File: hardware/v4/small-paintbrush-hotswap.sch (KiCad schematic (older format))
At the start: 17 parts, among them J1 Conn_01x02, J2 Conn_01x04, J3 Conn_01x04, SW1 SW_SPDT, SW2 SW_SPDT, U1 ProMicro, U2 ProMicro

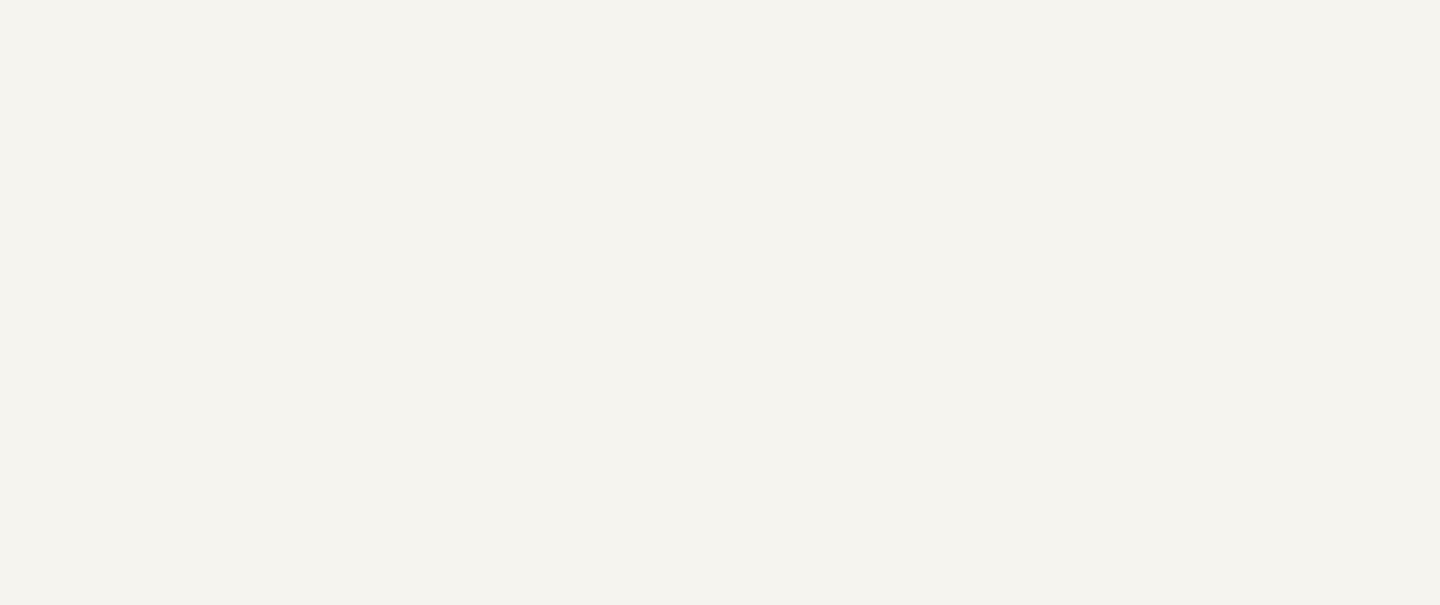
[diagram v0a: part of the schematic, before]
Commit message: Rev v4 to add tap holes
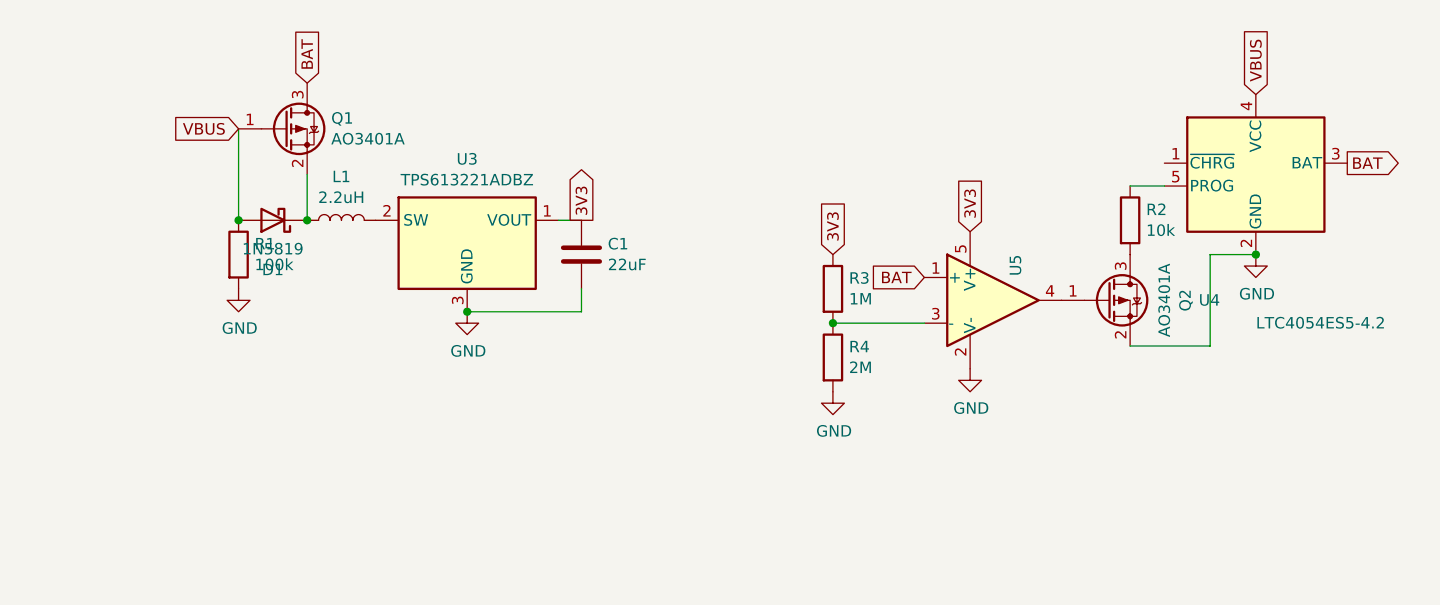
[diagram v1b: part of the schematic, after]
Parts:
- added C1: 22uF, symbol Device:C
- added D1: 1N5819, Diode_THT:D_DO-41_SOD81_P10.16mm_Horizontal, symbol Diode:1N5819
- added L1: 2.2uH, symbol Device:L
- added Q1, Q2: AO3401A, Package_TO_SOT_SMD:SOT-23, symbol Transistor_FET:AO3401A
- added R1: 100k, symbol Device:R
- added R2: 10k, symbol Device:R
- added R3: 1M, symbol Device:R
- added R4: 2M, symbol Device:R
- added U3: TPS613221ADBZ, Package_TO_SOT_SMD:SOT-23, symbol Regulator_Switching:TPS613221ADBZ
- added U4: LTC4054ES5-4.2, Package_TO_SOT_SMD:TSOT-23-5, symbol Battery_Management:LTC4054ES5-4.2
- added U5: LMV7271, symbol Comparator:LMV7271
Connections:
- net GND: now also C1.2, Q2.2 (S), R1.2, R4.2, U3.3 (GND), U4.2 (GND), U5.2 (V-)
- new net: L1.2, U3.2 (SW)
- new net: D1.1 (K), L1.1, Q1.2 (S)
- new net: R3.2, R4.1, U5.3 (-)
- new net: Q2.1 (G), U5.4
- new net: R2.1, U4.5 (PROG)
- new net: Q2.3 (D), R2.2
- new net 3V3: C1.1, R3.1, U3.1 (VOUT), U5.5 (V+)
- new net BAT: Q1.3 (D), U4.3 (BAT), U5.1 (+)
- new net VBUS: D1.2 (A), Q1.1 (G), R1.1, U4.4 (VCC)
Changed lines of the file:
@@
 Text GLabel 3350 5250 2    50   Input ~ 0
 RST
+$Comp
+L Regulator_Switching:TPS613221ADBZ U3
+U 1 1 604A5D63
+P 13450 2900
+F 0 "U3" H 13450 3267 50  0000 C CNN
+F 1 "TPS613221ADBZ" H 13450 3176 50  0000 C CNN
+F 2 "Package_TO_SOT_SMD:SOT-23" H 13450 2100 50  0001 C CNN
+F 3 "http://www.ti.com/lit/ds/symlink/tps61322.pdf" H 13450 2750 50  0001 C CNN
+	1    13450 2900
+	1    0    0    -1
+$EndComp
+$Comp
+L Device:L L1
+U 1 1 604A720D
+P 12900 2800
+F 0 "L1" V 13090 2800 50  0000 C CNN
+F 1 "2.2uH" V 12999 2800 50  0000 C CNN
+F 2 "" H 12900 2800 50  0001 C CNN
+F 3 "~" H 12900 2800 50  0001 C CNN
+	1    12900 2800
+	0    -1   -1   0
+$EndComp
+$Comp
+L power:GND #PWR09
+U 1 1 604AEF0B
+P 13450 3200
+F 0 "#PWR09" H 13450 2950 50  0001 C CNN
+F 1 "GND" H 13455 3027 50  0000 C CNN
+F 2 "" H 13450 3200 50  0001 C CNN
+F 3 "" H 13450 3200 50  0001 C CNN
+	1    13450 3200
+	1    0    0    -1
+$EndComp
+$Comp
+L Device:C C1
+U 1 1 604B0166
+P 13950 2950
+F 0 "C1" H 14065 2996 50  0000 L CNN
+F 1 "22uF" H 14065 2905 50  0000 L CNN
+F 2 "" H 13988 2800 50  0001 C CNN
+F 3 "~" H 13950 2950 50  0001 C CNN
+	1    13950 2950
+	1    0    0    -1
+$EndComp
+Wire Wire Line
+	13850 2800 13950 2800
+Wire Wire Line
+	13450 3200 13950 3200
+Wire Wire Line
+	13950 3200 13950 3100
+Connection ~ 13450 3200
+$Comp
+L Transistor_FET:AO3401A Q1
+U 1 1 604B65CA
+P 12650 2400
+F 0 "Q1" H 12855 2446 50  0000 L CNN
+F 1 "AO3401A" H 12855 2355 50  0000 L CNN
+F 2 "Package_TO_SOT_SMD:SOT-23" H 12850 2325 50  0001 L CIN
+F 3 "http://www.aosmd.com/pdfs/datasheet/AO3401A.pdf" H 12650 2400 50  0001 L CNN
+	1    12650 2400
+	1    0    0    -1
+$EndComp
+$Comp
+L Device:R R1
+U 1 1 604B844C
+P 12450 2950
+F 0 "R1" H 12520 2996 50  0000 L CNN
+F 1 "100k" H 12520 2905 50  0000 L CNN
+F 2 "" V 12380 2950 50  0001 C CNN
+F 3 "~" H 12450 2950 50  0001 C CNN
+	1    12450 2950
+	1    0    0    -1
+$EndComp
+$Comp
+L Diode:1N5819 D1
+U 1 1 604B9DBC
+P 12600 2800
+F 0 "D1" H 12600 3017 50  0000 C CNN
+F 1 "1N5819" H 12600 2926 50  0000 C CNN
+F 2 "Diode_THT:D_DO-41_SOD81_P10.16mm_Horizontal" H 12600 2625 50  0001 C CNN
+F 3 "http://www.vishay.com/docs/88525/1n5817.pdf" H 12600 2800 50  0001 C CNN
+	1    12600 2800
+	-1   0    0    1
+$EndComp
+$Comp
+L power:GND #PWR08
+U 1 1 604BBE27
+P 12450 3100
+F 0 "#PWR08" H 12450 2850 50  0001 C CNN
+F 1 "GND" H 12455 2927 50  0000 C CNN
+F 2 "" H 12450 3100 50  0001 C CNN
+F 3 "" H 12450 3100 50  0001 C CNN
+	1    12450 3100
+	1    0    0    -1
+$EndComp
+Wire Wire Line
+	12750 2600 12750 2800
+Wire Wire Line
+	12450 2400 12450 2800
+Text GLabel 12750 2200 1    50   Input ~ 0
+BAT
+Text GLabel 12450 2400 0    50   Input ~ 0
+VBUS
+Text GLabel 13950 2800 1    50   Output ~ 0
+3V3
+Text GLabel 15650 2850 1    50   Input ~ 0
+3V3
+$Comp
+L power:GND #PWR011
+U 1 1 604CFB18
+P 15650 3450
+F 0 "#PWR011" H 15650 3200 50  0001 C CNN
+F 1 "GND" H 15655 3277 50  0000 C CNN
+F 2 "" H 15650 3450 50  0001 C CNN
+F 3 "" H 15650 3450 50  0001 C CNN
+	1    15650 3450
+	1    0    0    -1
+$EndComp
+Text GLabel 15050 2950 1    50   Input ~ 0
+3V3
+Text GLabel 15450 3050 0    50   Input ~ 0
+BAT
+$Comp
+L Battery_Management:LTC4054ES5-4.2 U4
+U 1 1 604D2D35
+P 16900 2550
+F 0 "U4" H 16650 1950 50  0000 L CNN
+F 1 "LTC4054ES5-4.2" H 16900 1850 50  0000 L CNN
+F 2 "Package_TO_SOT_SMD:TSOT-23-5" H 16900 2050 50  0001 C CNN
+F 3 "https://www.analog.com/media/en/technical-documentation/data-sheets/405442xf.pdf" H 16900 2450 50  0001 C CNN
+	1    16900 2550
+	1    0    0    -1
+$EndComp
+$Comp
+L power:GND #PWR010
+U 1 1 604D3451
+P 16900 2950
+F 0 "#PWR010" H 16900 2700 50  0001 C CNN
+F 1 "GND" H 16905 2777 50  0000 C CNN
+F 2 "" H 16900 2950 50  0001 C CNN
+F 3 "" H 16900 2950 50  0001 C CNN
+	1    16900 2950
+	1    0    0    -1
+$EndComp
+$Comp
+L Device:R R2
+U 1 1 604D4E98
+P 16350 2800
+F 0 "R2" H 16420 2846 50  0000 L CNN
+F 1 "10k" H 16420 2755 50  0000 L CNN
+F 2 "" V 16280 2800 50  0001 C CNN
+F 3 "~" H 16350 2800 50  0001 C CNN
+	1    16350 2800
+	1    0    0    -1
+$EndComp
+Wire Wire Line
+	16500 2650 16350 2650
+Text GLabel 16900 2250 1    50   Input ~ 0
+VBUS
+$Comp
+L Comparator:LMV7271 U5
+U 1 1 604CD21E
+P 15750 3150
+F 0 "U5" V 15850 3350 50  0000 R CNN
+F 1 "LMV7271" H 16094 3105 50  0001 L CNN
+F 2 "" H 15750 3250 50  0001 C CNN
+F 3 "http://www.ti.com/lit/ds/symlink/lmv7271.pdf" H 15750 3350 50  0001 C CNN
+	1    15750 3150
+	1    0    0    -1
+$EndComp
+Text GLabel 17300 2550 2    50   Output ~ 0
+BAT
+$Comp
+L Device:R R3
+U 1 1 605159B5
+P 15050 3100
+F 0 "R3" H 15120 3146 50  0000 L CNN
+F 1 "1M" H 15120 3055 50  0000 L CNN
+F 2 "" V 14980 3100 50  0001 C CNN
+F 3 "~" H 15050 3100 50  0001 C CNN
+	1    15050 3100
+	1    0    0    -1
+$EndComp
+$Comp
+L Device:R R4
+U 1 1 6051C0A9
+P 15050 3400
+F 0 "R4" H 15120 3446 50  0000 L CNN
+F 1 "2M" H 15120 3355 50  0000 L CNN
+F 2 "" V 14980 3400 50  0001 C CNN
+F 3 "~" H 15050 3400 50  0001 C CNN
+	1    15050 3400
+	1    0    0    -1
+$EndComp
+$Comp
+L power:GND #PWR012
+U 1 1 6051C6FA
+P 15050 3550
+F 0 "#PWR012" H 15050 3300 50  0001 C CNN
+F 1 "GND" H 15055 3377 50  0000 C CNN
+F 2 "" H 15050 3550 50  0001 C CNN
+F 3 "" H 15050 3550 50  0001 C CNN
+	1    15050 3550
+	1    0    0    -1
+$EndComp
+$Comp
+L Transistor_FET:AO3401A Q2
+U 1 1 60542AAC
+P 16250 3150
+F 0 "Q2" V 16592 3150 50  0000 C CNN
+F 1 "AO3401A" V 16501 3150 50  0000 C CNN
+F 2 "Package_TO_SOT_SMD:SOT-23" H 16450 3075 50  0001 L CIN
+F 3 "http://www.aosmd.com/pdfs/datasheet/AO3401A.pdf" H 16250 3150 50  0001 L CNN
+	1    16250 3150
+	1    0    0    -1
+$EndComp
+Connection ~ 12750 2800
+Connection ~ 12450 2800
+Wire Wire Line
+	16350 3350 16700 3350
+Wire Wire Line
+	16700 3350 16700 2950
+Wire Wire Line
+	16700 2950 16900 2950
+Connection ~ 16900 2950
+Wire Wire Line
+	15050 3250 15450 3250
+Connection ~ 15050 3250
 $EndSCHEMATC
